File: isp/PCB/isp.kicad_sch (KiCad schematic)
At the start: 19 parts, among them J1 PC, J2 12V, J3 AVR-ISP-6, J4 POW_SEL, J5 USART, Q1 2N7002, Q2 2N7002, Q3 2N7002, U1 ATtiny25-20P

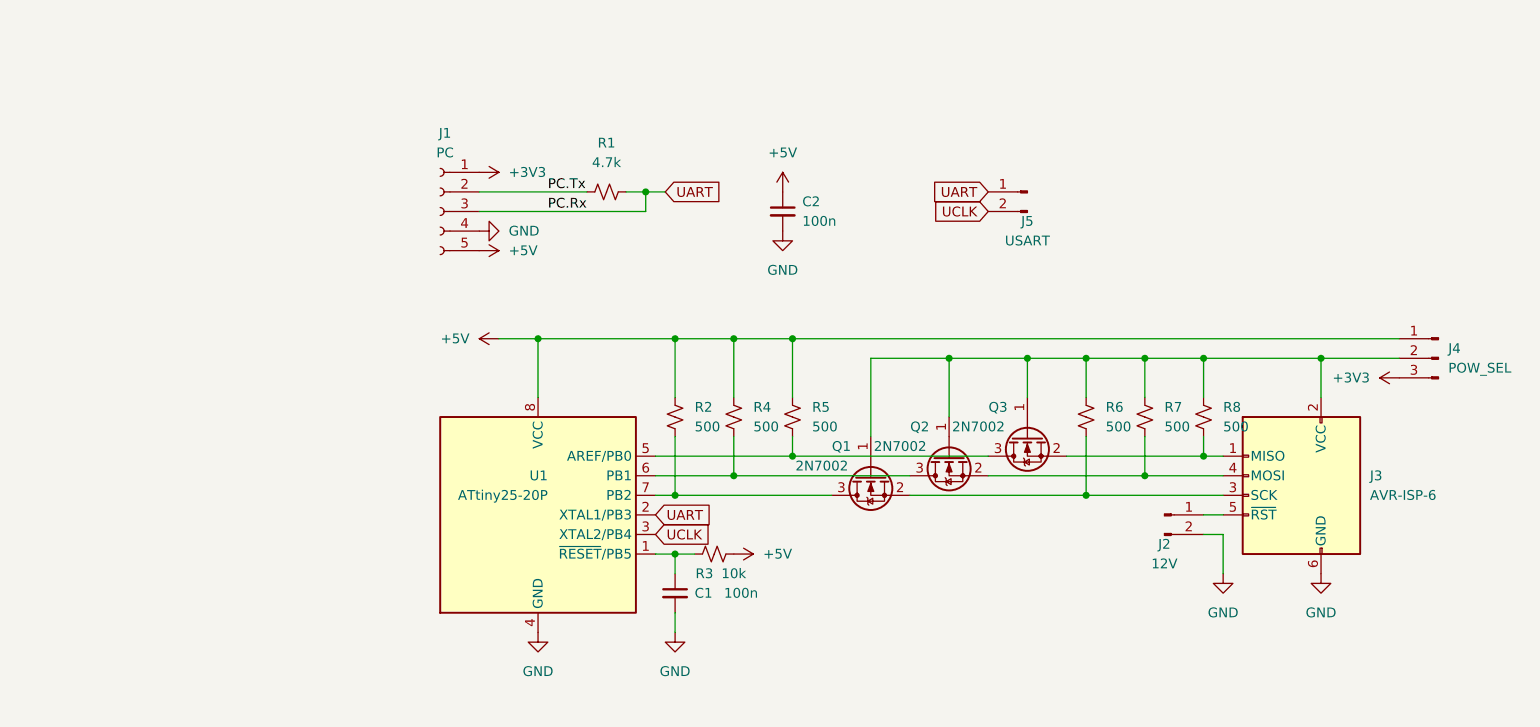
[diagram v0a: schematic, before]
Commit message: Optimize ISP circuit - Add ISP reset button and target enable SW - Change ISP output level shifter from NMOS to diode (save space & cost) - Rearrang PCB to save size, some SMD on back can overlap with USB board - Add a LED
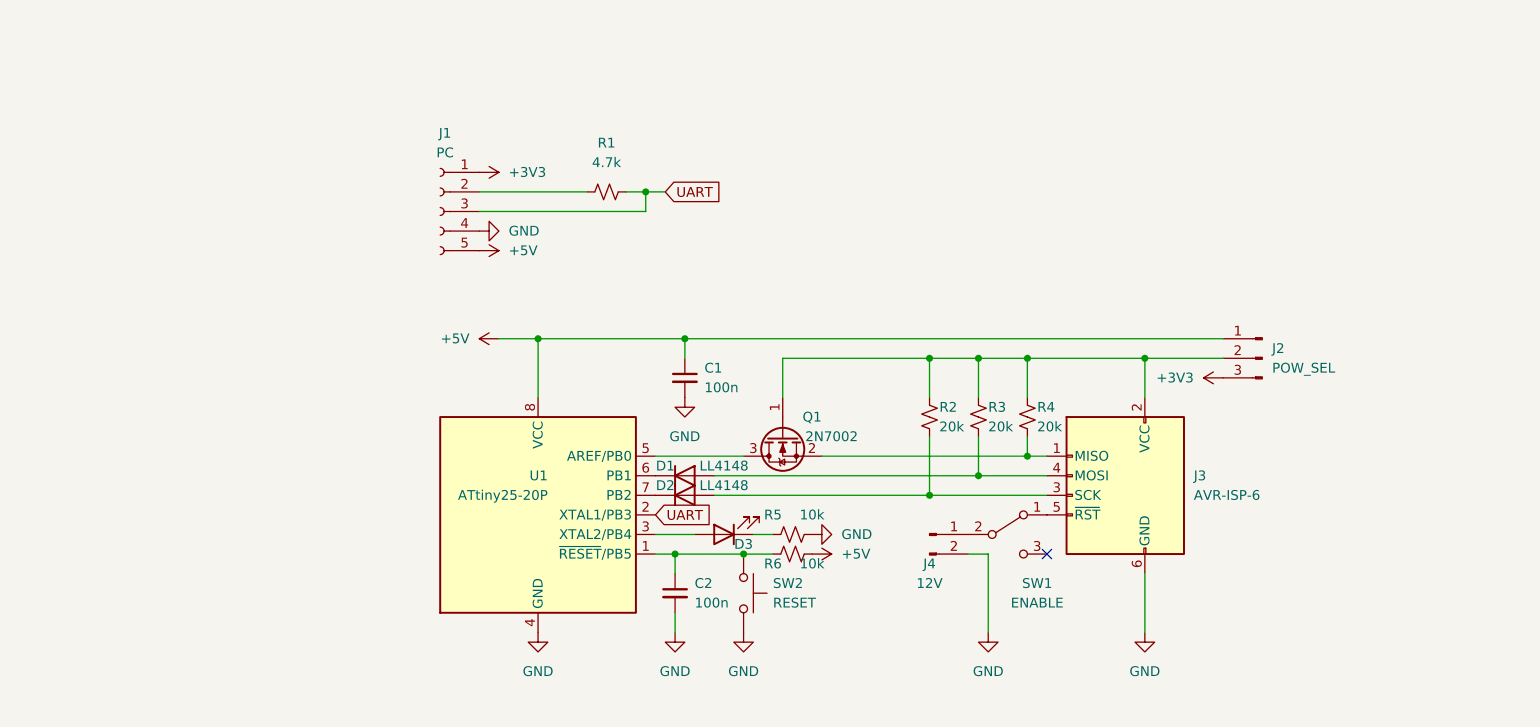
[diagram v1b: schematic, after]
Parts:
- removed J5: USART, Connector_PinHeader_2.54mm:PinHeader_1x02_P2.54mm_Vertical, symbol Connector:Conn_01x02_Pin
- removed Q2, Q3: 2N7002, Package_TO_SOT_SMD:SOT-23, symbol Transistor_FET:2N7002
- removed R2, R8: 500, Resistor_SMD:R_0805_2012Metric, symbol Device:R_Small_US
- added D1, D2: LL4148, Diode_SMD:D_MiniMELF, symbol Diode:LL4448
- added D3: LED, LED_SMD:LED_0805_2012Metric, symbol Device:LED
- added SW1: ENABLE, Button_Switch_THT:SW_Slide_1P2T_CK_OS102011MS2Q, symbol Switch:SW_SPDT
- added SW2: RESET, Button_Switch_SMD:SW_Tactile_SPST_NO_Straight_CK_PTS636Sx25SMTRLFS, symbol Switch:SW_Push
- R2: renamed from R6; value 500 -> 20k
- R3: renamed from R7; value 500 -> 20k
- R4: value 500 -> 20k
- R5: value 500 -> 10k
- renumbered C2 to C1, C1 to C2, J4 to J2, J2 to J4, R3 to R6
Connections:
- net +5V: no longer R4.1, R5.1
- net GND: now also R5.2, SW2.2
- net at J2.2 (Pin_2), J3.2 (VCC), Q1.1 (G)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: now also R4.1
- net at J3.3 (SCK), R2.2: now also D2.2 (A); no longer Q1.2 (S)
- net at Q1.3 (D): now also U1.5 (AREF/PB0); no longer U1.7 (PB2)
- net at J3.1 (MISO): now also Q1.2 (S), R4.2
- net at J3.4 (MOSI), R3.2: now also D1.2 (A)
- net at J3.5 (~{RST}): now also SW1.1 (A); no longer J4.1 (Pin_1)
- net at C2.1, R6.1, U1.1 (~{RESET}/PB5): now also SW2.1
- net at U1.6 (PB1): now also D1.1 (K); no longer R4.2
- net PC.Tx: no longer names the net of J1.2 (Pin_2), R1.1
- net UCLK: no longer names the net of U1.3 (XTAL2/PB4)
- net UCLK: now also D3.2 (A)
- new net: D3.1 (K), R5.1
- new net: J4.1 (Pin_1), SW1.2 (B)
- new net: D2.1 (K), U1.7 (PB2)
- no-connect marks 0 -> 1
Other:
- company: Captdam -> (none)
- title: Tiny25ISP -> (none)
- moved on the sheet: C1, J2, J3, J4, R2, R3, R6

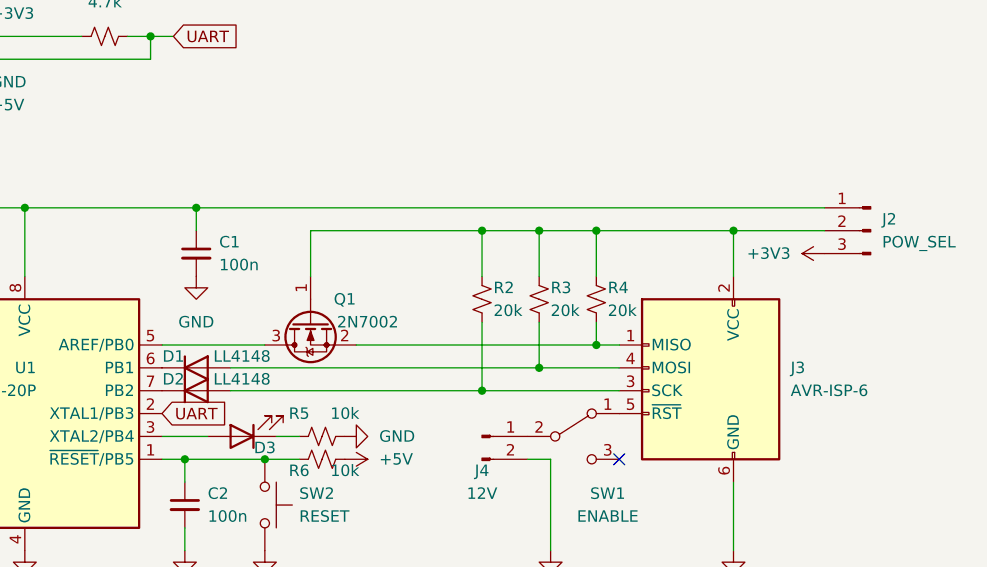
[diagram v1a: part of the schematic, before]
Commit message: ISP speed change: 9600 --> 115200 - Increase speed: Data stream (EEPROM/Flash) transfer at 9600BAUD is too slow (9600 only good for fuse). - Reduce resistor (50k --> 5k), Pull-up time too long for 50kR, OK for 1MHz but gives error when talk to 8MHz AVR. - Note: target AVR response to clk too fast. Signal propagation is not fast enough due to long rise time.
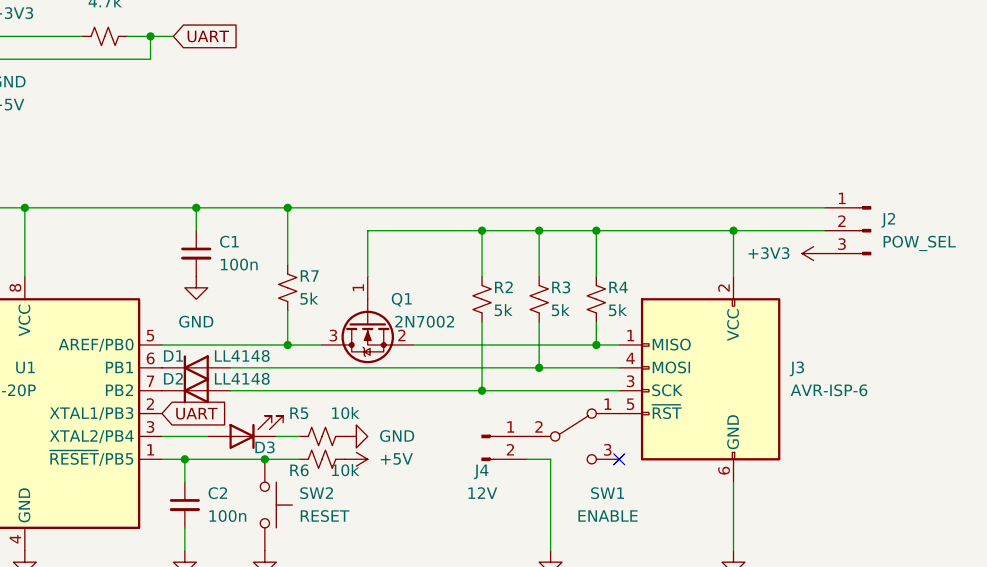
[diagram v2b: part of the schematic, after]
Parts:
- added R7: 5k, Resistor_SMD:R_0603_1608Metric, symbol Device:R_Small_US
- R2, R3, R4: value 20k -> 5k
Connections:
- net +5V: now also R7.1
- net at Q1.3 (D), U1.5 (AREF/PB0): now also R7.2
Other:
- moved on the sheet: Q1
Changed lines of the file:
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@@
   (junction (at 177.8 74.93) (diameter 0) (color 0 0 0 0)
   )
+  (junction (at 128.27 72.39) (diameter 0) (color 0 0 0 0)
+  )
   (junction (at 149.86 74.93) (diameter 0) (color 0 0 0 0)
   )
@@
   )
   (junction (at 113.03 53.34) (diameter 0) (color 0 0 0 0)
+  )
+  (junction (at 128.27 87.63) (diameter 0) (color 0 0 0 0)
   )
   (no_connect (at 165.1 100.33))
@@
     (stroke (width 0) (type default))
   )
-  (wire (pts (xy 114.3 87.63) (xy 125.73 87.63))
+  (wire (pts (xy 114.3 87.63) (xy 128.27 87.63))
     (stroke (width 0) (type default))
   )
@@
     (stroke (width 0) (type default))
   )
+  (wire (pts (xy 128.27 87.63) (xy 132.08 87.63))
+    (stroke (width 0) (type default))
+  )
   (wire (pts (xy 113.03 53.34) (xy 113.03 55.88))
     (stroke (width 0) (type default))
@@
     (stroke (width 0) (type default))
   )
-  (wire (pts (xy 118.11 72.39) (xy 187.96 72.39))
+  (wire (pts (xy 118.11 72.39) (xy 128.27 72.39))
+    (stroke (width 0) (type default))
+  )
+  (wire (pts (xy 128.27 72.39) (xy 128.27 78.74))
     (stroke (width 0) (type default))
   )
@@
     (stroke (width 0) (type default))
   )
-  (wire (pts (xy 130.81 74.93) (xy 149.86 74.93))
+  (wire (pts (xy 137.16 74.93) (xy 149.86 74.93))
     (stroke (width 0) (type default))
   )
@@
     (stroke (width 0) (type default))
   )
-  (wire (pts (xy 130.81 80.01) (xy 130.81 74.93))
-    (stroke (width 0) (type default))
-  )
-  (wire (pts (xy 135.89 87.63) (xy 162.56 87.63))
+  (wire (pts (xy 128.27 72.39) (xy 187.96 72.39))
+    (stroke (width 0) (type default))
+  )
+  (wire (pts (xy 137.16 80.01) (xy 137.16 74.93))
+    (stroke (width 0) (type default))
+  )
+  (wire (pts (xy 142.24 87.63) (xy 162.56 87.63))
+    (stroke (width 0) (type default))
+  )
+  (wire (pts (xy 128.27 83.82) (xy 128.27 87.63))
     (stroke (width 0) (type default))
   )
@@
       (effects (font (size 1.27 1.27)) (justify left))
     )
-    (property "Value" "20k" (at 151.13 83.82 0)
+    (property "Value" "5k" (at 151.13 83.82 0)
       (effects (font (size 1.27 1.27)) (justify left))
     )
@@
     )
   )
-  (symbol (lib_id "Transistor_FET:2N7002") (at 130.81 85.09 90) (mirror x) (unit 1)
-    (in_bom yes) (on_board yes) (dnp no)
-    (property "Reference" "Q1" (at 134.62 82.55 90)
-      (effects (font (size 1.27 1.27)))
-    )
-    (property "Value" "2N7002" (at 137.16 85.09 90)
-      (effects (font (size 1.27 1.27)))
-    )
-    (property "Footprint" "Package_TO_SOT_SMD:SOT-23" (at 132.715 90.17 0)
+  (symbol (lib_id "Transistor_FET:2N7002") (at 137.16 85.09 90) (mirror x) (unit 1)
+    (in_bom yes) (on_board yes) (dnp no)
+    (property "Reference" "Q1" (at 140.97 82.55 90)
+      (effects (font (size 1.27 1.27)))
+    )
+    (property "Value" "2N7002" (at 143.51 85.09 90)
+      (effects (font (size 1.27 1.27)))
+    )
+    (property "Footprint" "Package_TO_SOT_SMD:SOT-23" (at 139.065 90.17 0)
       (effects (font (size 1.27 1.27) italic) (justify left) hide)
     )
-    (property "Datasheet" "https://www.onsemi.com/pub/Collateral/NDS7002A-D.PDF" (at 130.81 85.09 0)
+    (property "Datasheet" "https://www.onsemi.com/pub/Collateral/NDS7002A-D.PDF" (at 137.16 85.09 0)
       (effects (font (size 1.27 1.27)) (justify left) hide)
     )
@@
       (effects (font (size 1.27 1.27)) (justify left))
     )
-    (property "Value" "20k" (at 163.83 83.82 0)
+    (property "Value" "5k" (at 163.83 83.82 0)
       (effects (font (size 1.27 1.27)) (justify left))
     )
@@
     )
   )
+  (symbol (lib_id "Device:R_Small_US") (at 128.27 81.28 0) (unit 1)
+    (in_bom yes) (on_board yes) (dnp no)
+    (property "Reference" "R7" (at 129.54 80.01 0)
+      (effects (font (size 1.27 1.27)) (justify left))
+    )
+    (property "Value" "5k" (at 129.54 82.55 0)
+      (effects (font (size 1.27 1.27)) (justify left))
+    )
+    (property "Footprint" "Resistor_SMD:R_0603_1608Metric" (at 128.27 81.28 0)
+      (effects (font (size 1.27 1.27)) hide)
+    )
+    (property "Datasheet" "~" (at 128.27 81.28 0)
+      (effects (font (size 1.27 1.27)) hide)
+    )
+    (pin "1")
+    (pin "2")
+    (instances
+      (project "isp"
+        (path "/73a66f9a-bf0c-4d1c-83de-95af1a15ee8d"
+          (reference "R7") (unit 1)
+        )
+      )
+    )
+  )
   (symbol (lib_id "power:GND") (at 118.11 80.01 0) (unit 1)
     (in_bom yes) (on_board yes) (dnp no) (fields_autoplaced)
@@
       (effects (font (size 1.27 1.27)) (justify left))
     )
-    (property "Value" "20k" (at 157.48 83.82 0)
-      (effects (font (size 1.27 1.27)) (justify left))
-    )
+    (property "Value" "5k" (at 157.48 83.82 0)
+      (effects (font (size 1.27 1.27)) (justify left))
+    )

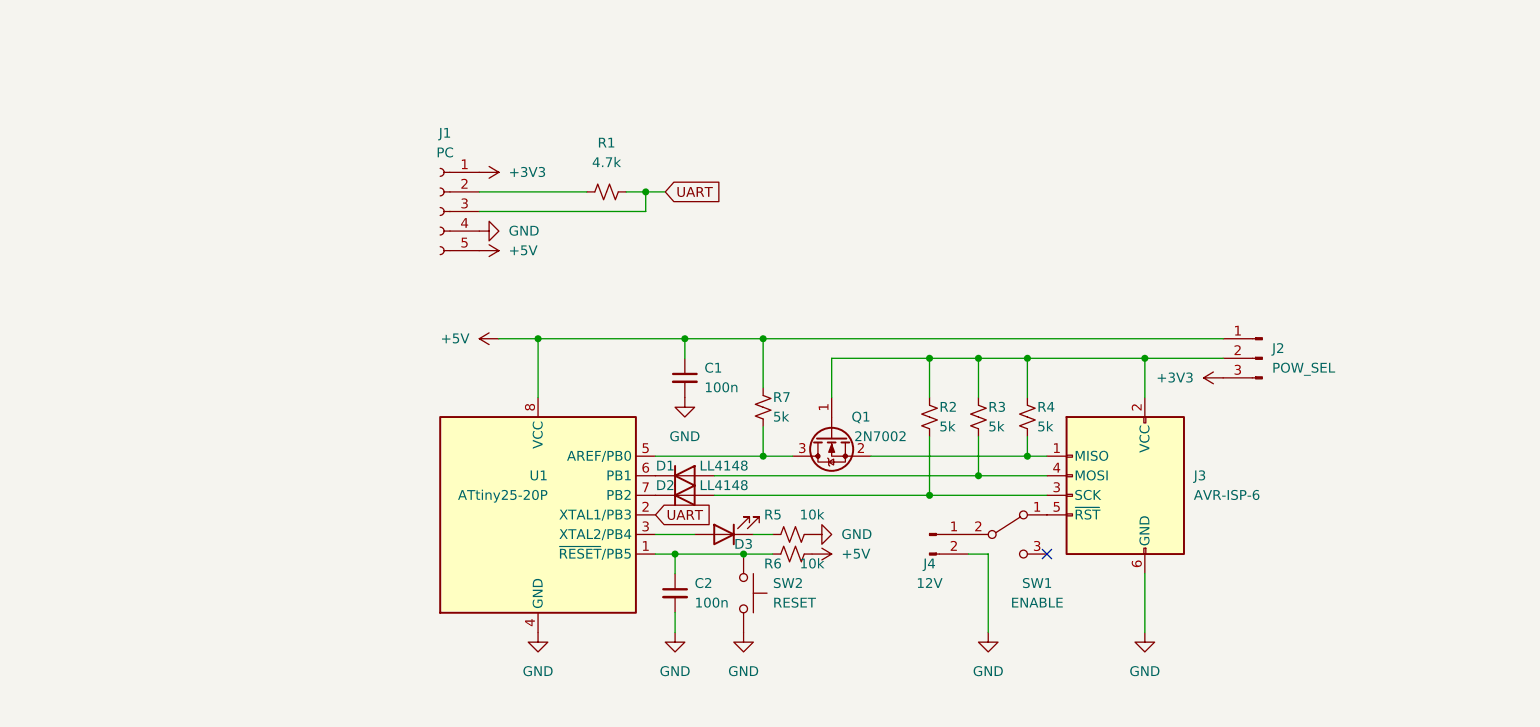
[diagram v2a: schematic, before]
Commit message: New PCB design: Switch from tiny25 to tiny441/841
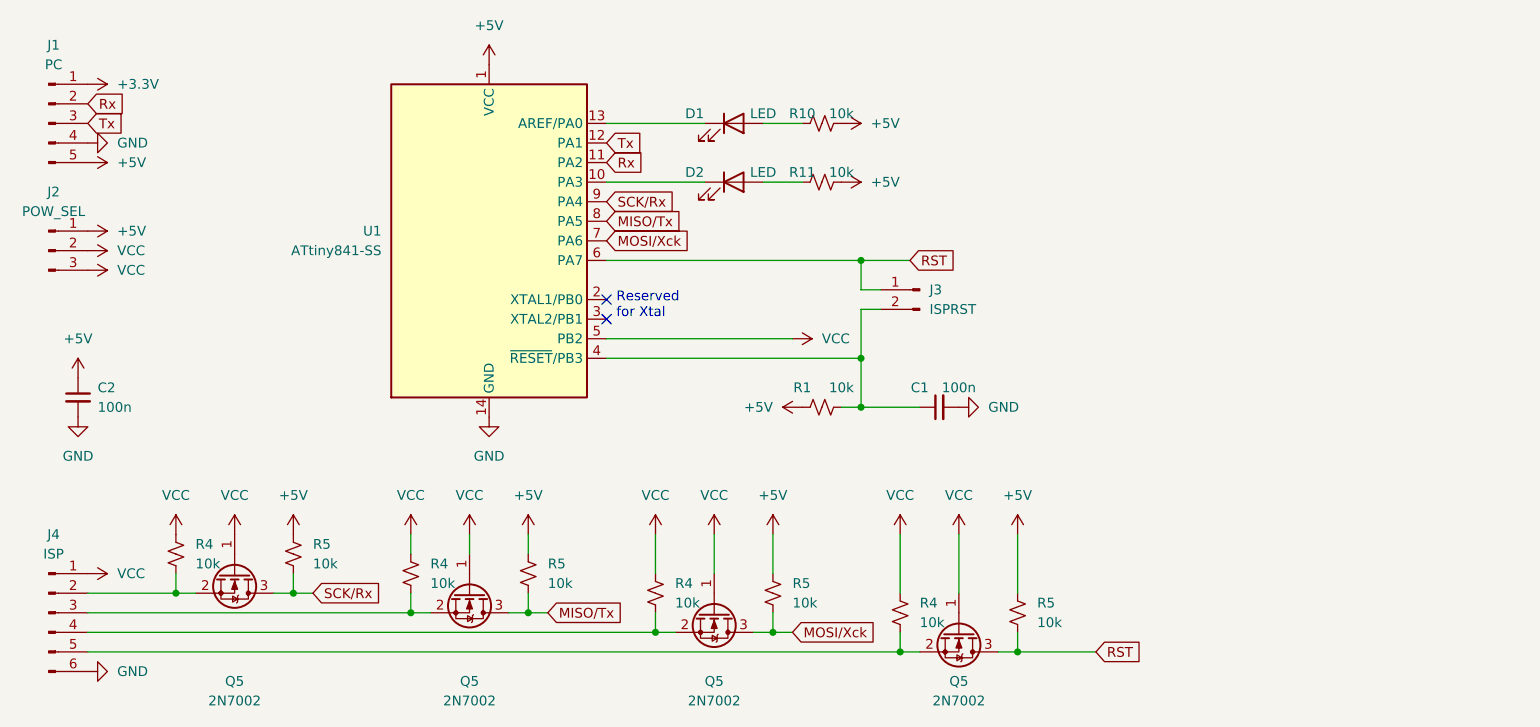
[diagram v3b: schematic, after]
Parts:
- removed D1, D2: LL4148, Diode_SMD:D_MiniMELF, symbol Diode:LL4448
- removed D3: LED, LED_SMD:LED_0805_2012Metric, symbol Device:LED
- removed J1: PC, Connector_PinSocket_2.54mm:PinSocket_1x05_P2.54mm_Vertical, symbol Connector:Conn_01x05_Female
- removed J2: POW_SEL, Connector_PinSocket_2.54mm:PinSocket_1x03_P2.54mm_Vertical, symbol Connector:Conn_01x03_Male
- removed J3: AVR-ISP-6, Connector_PinHeader_2.54mm:PinHeader_2x03_P2.54mm_Vertical, symbol Connector:AVR-ISP-6
- removed J4: 12V, Connector_PinHeader_2.54mm:PinHeader_1x02_P2.54mm_Vertical, symbol Connector:Conn_01x02_Pin
- removed Q1: 2N7002, Package_TO_SOT_SMD:SOT-23, symbol Transistor_FET:2N7002
- removed R2, R3, R4: 5k, Resistor_SMD:R_0805_2012Metric, symbol Device:R_Small_US
- removed R5, R6: 10k, Resistor_SMD:R_0805_2012Metric, symbol Device:R_Small_US
- removed R7: 5k, Resistor_SMD:R_0603_1608Metric, symbol Device:R_Small_US
- removed SW1: ENABLE, Button_Switch_THT:SW_Slide_1P2T_CK_OS102011MS2Q, symbol Switch:SW_SPDT
- removed SW2: RESET, Button_Switch_SMD:SW_Tactile_SPST_NO_Straight_CK_PTS636Sx25SMTRLFS, symbol Switch:SW_Push
- removed U1: ATtiny25-20P, Package_DIP:DIP-8_W7.62mm, symbol MCU_Microchip_ATtiny:ATtiny25-20P
- added D1, D2: LED, LED_SMD:LED_0805_2012Metric, symbol Device:LED
- added J1: PC, Connector_PinHeader_2.54mm:PinHeader_1x05_P2.54mm_Vertical, symbol Connector:Conn_01x05_Pin
- added J2: POW_SEL, Connector_PinHeader_2.54mm:PinHeader_1x03_P2.54mm_Vertical, symbol Connector:Conn_01x03_Pin
- added J3: ISPRST, Connector_PinHeader_2.54mm:PinHeader_1x02_P2.54mm_Vertical, symbol Connector:Conn_01x02_Pin
- added J4: ISP, Connector_PinHeader_2.54mm:PinHeader_1x06_P2.54mm_Vertical, symbol Connector:Conn_01x06_Pin
- added Q5 (x4): 2N7002, Package_TO_SOT_SMD:SOT-23, symbol Transistor_FET:2N7002
- added R10, R11, R4 (x4), R5 (x4): 10k, Resistor_SMD:R_0805_2012Metric, symbol Device:R_Small_US
- added U1: ATtiny841-SS, Package_SO:SOIC-14_3.9x8.7mm_P1.27mm, symbol MCU_Microchip_ATtiny:ATtiny841-SS
- R1: value 4.7k -> 10k
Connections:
- net +5V: now also C2.1, R1.1, J1.5 (Pin_5), J2.1 (Pin_1), R10.2, R11.2, R5.1, R5.1, R5.1, R5.1, U1.1 (VCC); no longer C1.1
- net GND: now also J1.4 (Pin_4), J4.6 (Pin_6), U1.14 (GND)
- net UART: no longer names the net of R1.2
- net UART: now also C1.1, J3.2 (Pin_2), U1.4 (~{RESET}/PB3)
- new net: J4.2 (Pin_2), Q5.2 (S), R4.2
- new net: J4.4 (Pin_4), Q5.2 (S), R4.2
- new net: D2.1 (K), U1.10 (PA3)
- new net: D1.1 (K), U1.13 (AREF/PA0)
- new net: J4.5 (Pin_5), Q5.2 (S), R4.2
- new net: J4.3 (Pin_3), Q5.2 (S), R4.2
- new net: D2.2 (A), R11.1
- new net: D1.2 (A), R10.1
- new net +3.3V: J1.1 (Pin_1)
- new net MISO/Tx: Q5.3 (D), R5.2, U1.8 (PA5)
- new net MOSI/Xck: Q5.3 (D), R5.2, U1.7 (PA6)
- new net RST: J3.1 (Pin_1), Q5.3 (D), R5.2, U1.6 (PA7)
- new net Rx: J1.2 (Pin_2), U1.11 (PA2)
- new net SCK/Rx: Q5.3 (D), R5.2, U1.9 (PA4)
- new net Tx: J1.3 (Pin_3), U1.12 (PA1)
- new net VCC: J2.2 (Pin_2), J2.3 (Pin_3), J4.1 (Pin_1), Q5.1 (G), Q5.1 (G), Q5.1 (G), Q5.1 (G), R4.1, R4.1, R4.1, R4.1, U1.5 (PB2)
- no-connect marks 1 -> 2
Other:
- note added: "Reserved for Xtal"
